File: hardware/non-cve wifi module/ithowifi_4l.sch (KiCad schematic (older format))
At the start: 47 parts, among them J1 USB_B_Micro, J2 RJ45_LED_Shielded, J3 Conn_Coaxial, J4 Conn_02x02_Odd_Even, J5 Conn_02x02_Odd_Even, J6 Conn_01x02_Male, Q1 BSS138, Q2 BSS138, Q3 BC847, Q4 BC847, SW1 Fail safe, U1 ESP32-WROOM, U2 CC1101-868MHz-Module, U3 CH340G, U4 AMS1117-3.3, Y1 Crystal_GND24_Small

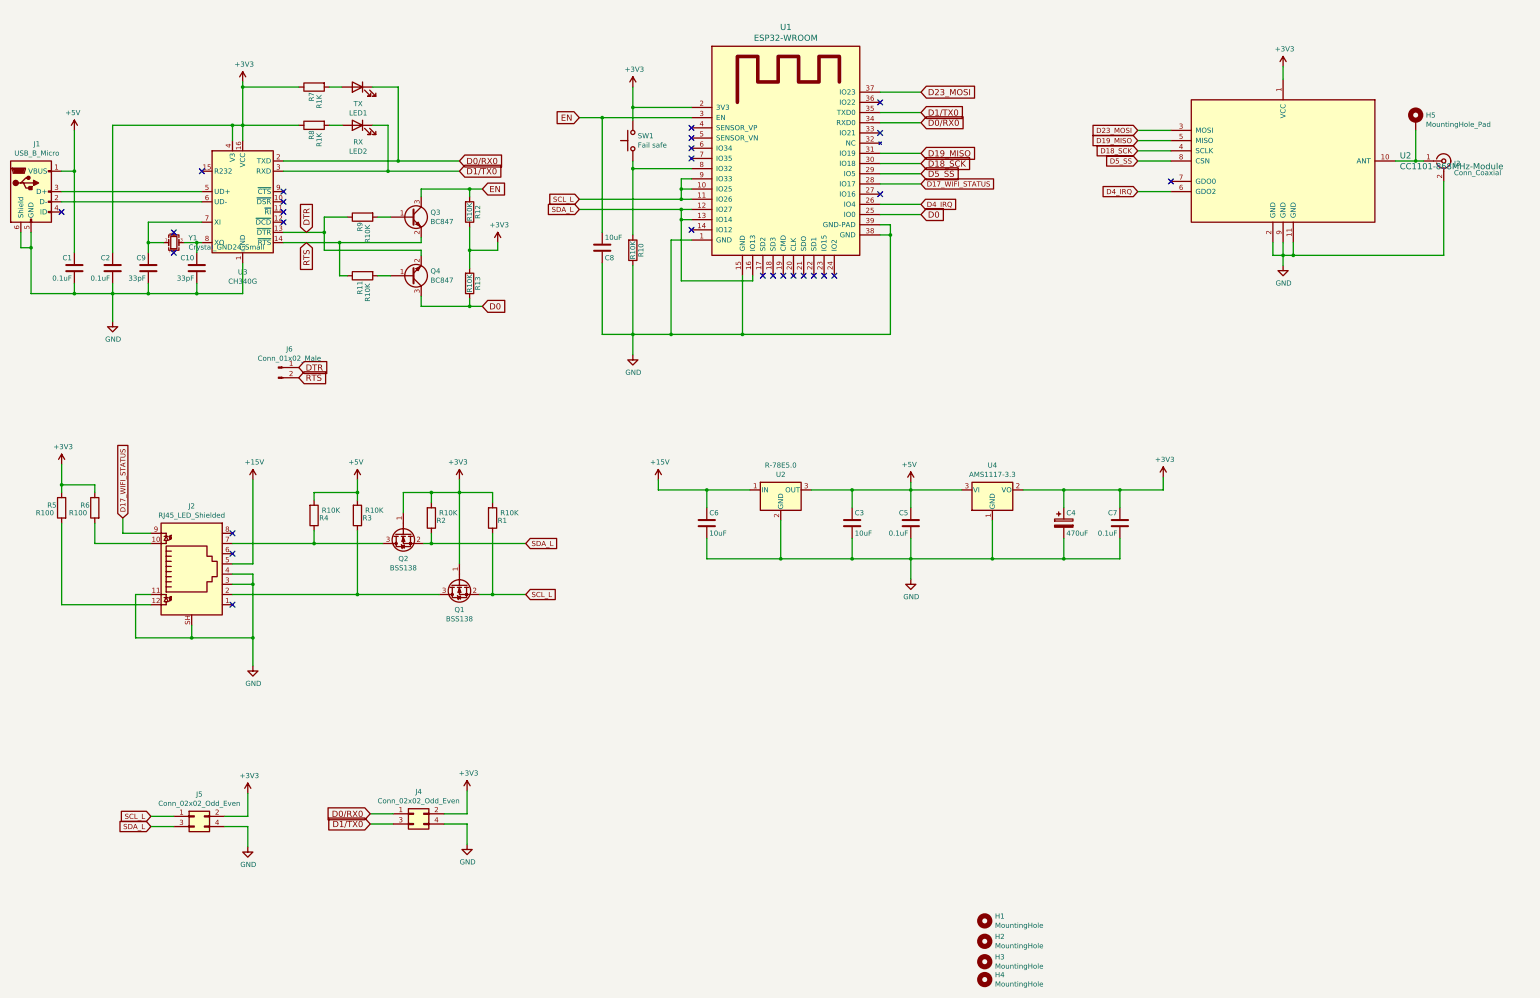
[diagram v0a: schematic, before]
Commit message: Version 2.3-beta5
- fix: prevent crashes unsupported or partly supported itho devices
- breaking: On the up-side; all settings and labels have been regenerated and checked (and some translated) with a script, units have been added where available and labels are more descriptive. On the flip-side; automations based on the API, specifically the itho status label based automations might need to be updated.
- add: support for itho HeatPumt (WPU) devices and AutoTemp devices.

Please check labels for status and settings, if you see anything wrong, please let me know.
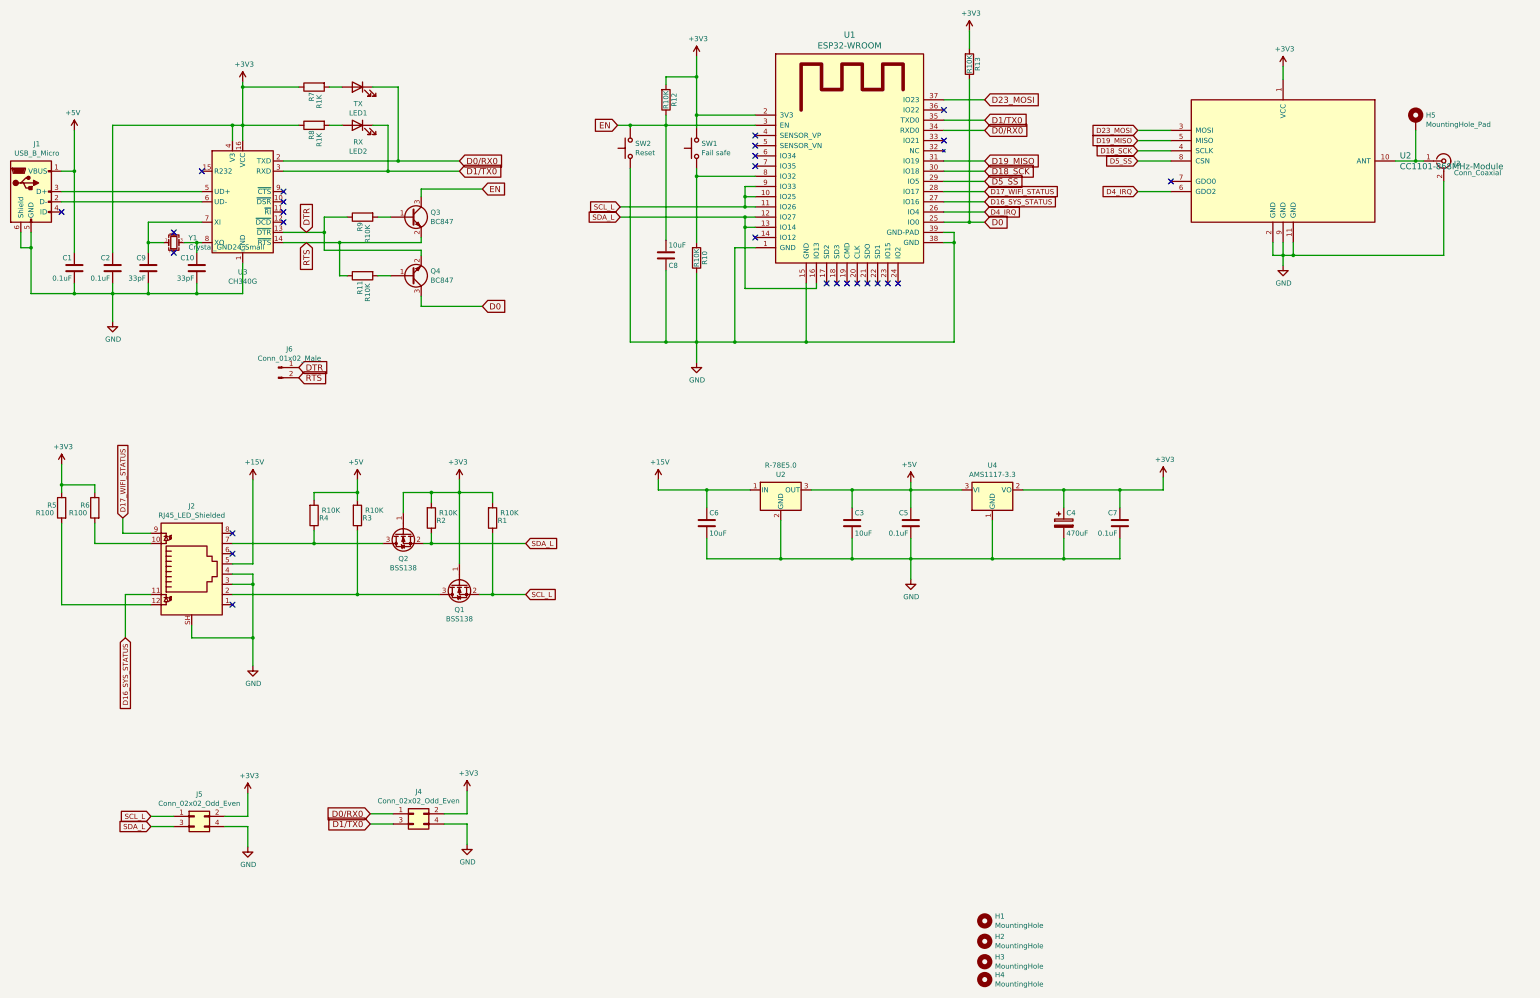
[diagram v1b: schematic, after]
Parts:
- added SW2: Reset, nrg_watch:TS-1187, symbol Switch:SW_Push
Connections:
- net +3V3: now also R12.2; no longer R12.1
- net EN: now also R12.1, SW2.2; no longer R12.2
- net GND: now also SW2.1; no longer J2.11
- net D16_SYS_STATUS: now reaches U1.27 (IO16)
- net D16_SYS_STATUS: now also J2.11
- no-connect marks 28 -> 27
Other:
- moved on the sheet: C8, R10, R12, R13, SW1, U1

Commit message: Update HW files and correct spelling
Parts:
- removed J6: Conn_01x02_Male, Connector_PinHeader_2.54mm:PinHeader_1x02_P2.54mm_Vertical, symbol Connector:Conn_01x02_Male
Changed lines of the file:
@@
 Wire Wire Line
 	14525 2450 14600 2450
-$Comp
-L Connector:Conn_01x02_Male J6
-U 1 1 61A92742
-P 3375 4475
-F 0 "J6" H 3483 4656 50  0000 C CNN
-F 1 "Conn_01x02_Male" H 3483 4565 50  0000 C CNN
-F 2 "Connector_PinHeader_2.54mm:PinHeader_1x02_P2.54mm_Vertical" H 3375 4475 50  0001 C CNN
-F 3 "~" H 3375 4475 50  0001 C CNN
-	1    3375 4475
-	1    0    0    -1
-$EndComp
 Wire Wire Line
 	3425 3250 3975 3250
@@
 Text GLabel 3650 3250 3    60   Input ~ 0
 RTS
-Text GLabel 3575 4575 2    60   Input ~ 0
-RTS
-Text GLabel 3575 4475 2    60   Input ~ 0
-DTR
 NoConn ~ 1250 2950
 NoConn ~ 2925 6100

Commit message: Update hardware design files
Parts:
- added J6: Conn_01x02_Male, Connector_PinHeader_2.54mm:PinHeader_1x02_P2.54mm_Vertical, symbol Connector:Conn_01x02_Male
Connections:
- net DTR: now also J6.1 (Pin_1)
- net RTS: now also J6.2 (Pin_2)
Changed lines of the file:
@@
 Wire Wire Line
 	14525 2450 14600 2450
+$Comp
+L Connector:Conn_01x02_Male J6
+U 1 1 61A92742
+P 3375 4475
+F 0 "J6" H 3483 4656 50  0000 C CNN
+F 1 "Conn_01x02_Male" H 3483 4565 50  0000 C CNN
+F 2 "Connector_PinHeader_2.54mm:PinHeader_1x02_P2.54mm_Vertical" H 3375 4475 50  0001 C CNN
+F 3 "~" H 3375 4475 50  0001 C CNN
+	1    3375 4475
+	1    0    0    -1
+$EndComp
 Wire Wire Line
 	3425 3250 3975 3250
@@
 Text GLabel 3650 3250 3    60   Input ~ 0
 RTS
+Text GLabel 3575 4575 2    60   Input ~ 0
+RTS
+Text GLabel 3575 4475 2    60   Input ~ 0
+DTR
 NoConn ~ 1250 2950
 NoConn ~ 2925 6100
